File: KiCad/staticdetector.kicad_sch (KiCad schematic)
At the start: 15 parts, among them J1 Conn_01x04, Q1 Q_NMOS_GDS_2SK4033, Q2 Q_NPN_BEC_2PD601ART, Q3 Q_NPN_BCE_2SCR533P, SW1 SW_Push

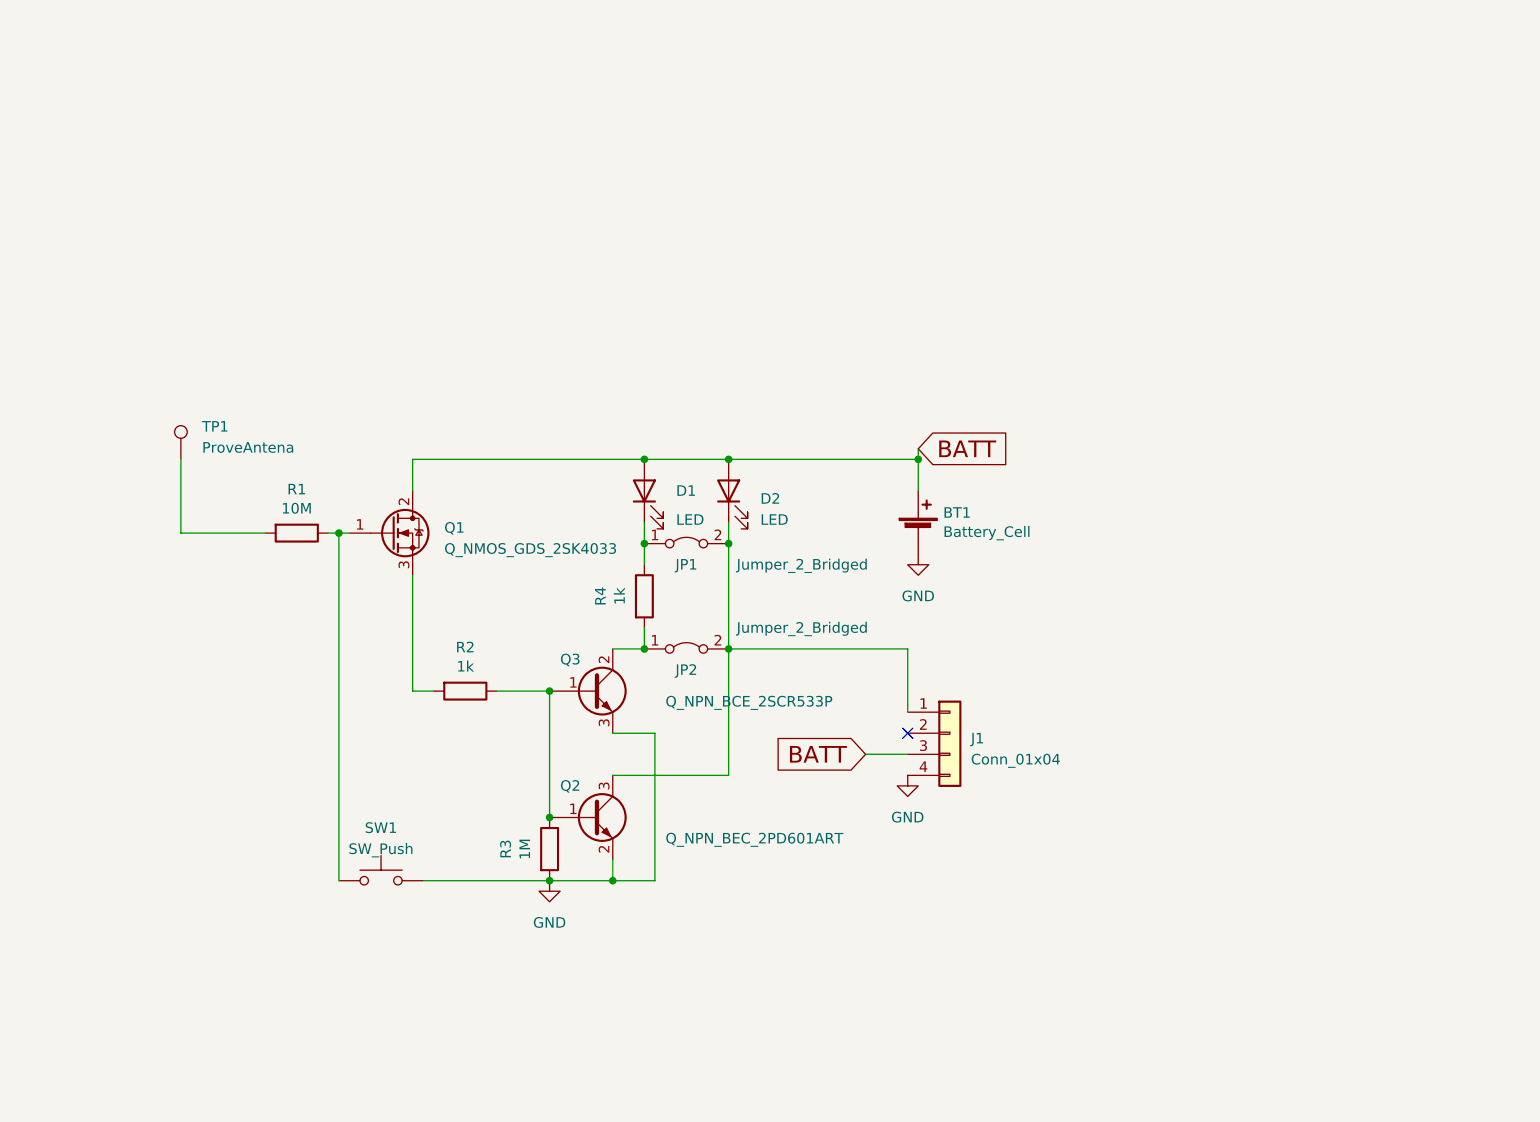
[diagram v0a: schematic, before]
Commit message: change file to OPAMP version
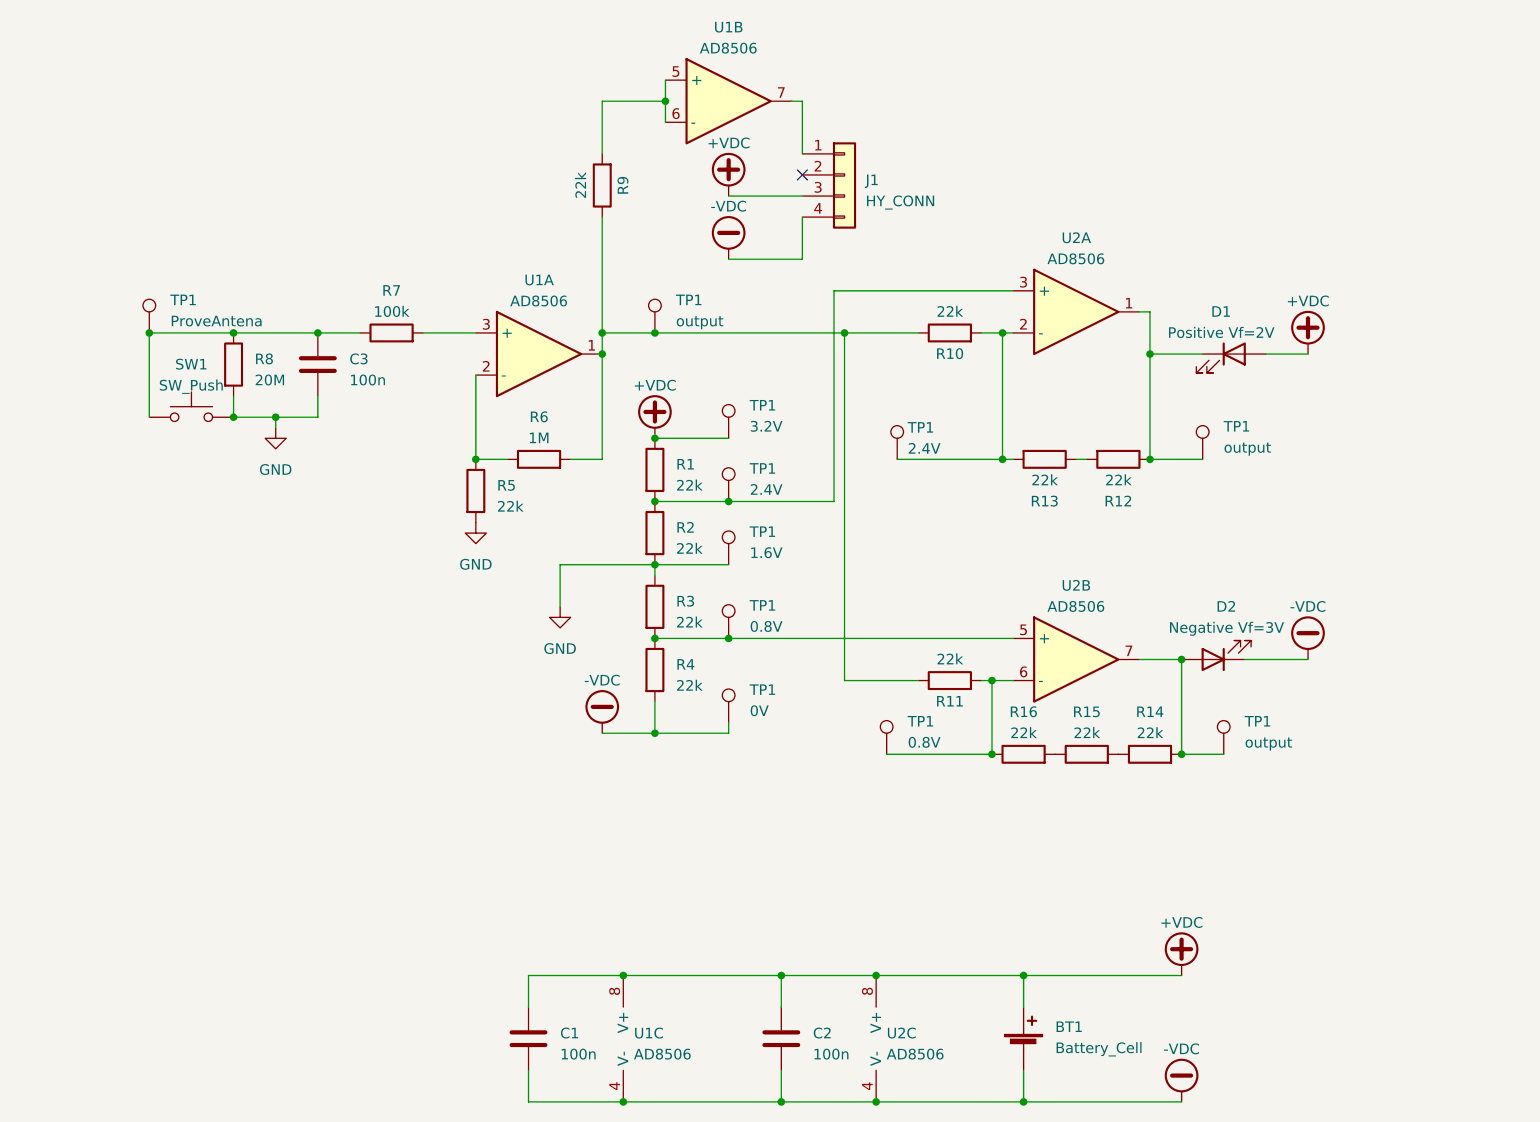
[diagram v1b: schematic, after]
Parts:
- removed JP1, JP2: Jumper_2_Bridged, Jumper:SolderJumper-2_P1.3mm_Bridged_RoundedPad1.0x1.5mm, symbol Jumper:Jumper_2_Bridged
- removed Q1: Q_NMOS_GDS_2SK4033, Package_TO_SOT_SMD:TO-252-2, symbol Device:Q_NMOS_GDS
- removed Q2: Q_NPN_BEC_2PD601ART, Package_TO_SOT_SMD:SOT-23W, symbol Device:Q_NPN_BEC
- removed Q3: Q_NPN_BCE_2SCR533P, Package_TO_SOT_SMD:SOT-89-3, symbol Device:Q_NPN_BCE
- removed TP1: ProveAntena, TestPoint:TestPoint_Pad_D4.0mm, symbol Connector:TestPoint
- added C1, C2, C3: 100n, Capacitor_SMD:C_1206_3216Metric_Pad1.33x1.80mm_HandSolder, symbol Device:C
- added R10, R11, R12, R13, R14, R15, R16, R5, R9: 22k, Resistor_SMD:R_1206_3216Metric_Pad1.30x1.75mm_HandSolder, symbol Device:R
- added R6: 1M, Resistor_SMD:R_1206_3216Metric_Pad1.30x1.75mm_HandSolder, symbol Device:R
- added R7: 100k, Resistor_SMD:R_1206_3216Metric_Pad1.30x1.75mm_HandSolder, symbol Device:R
- added R8: 20M, Resistor_SMD:R_1206_3216Metric_Pad1.30x1.75mm_HandSolder, symbol Device:R
- added TP1 (x2): 0.8V, TestPoint:TestPoint_Loop_D1.80mm_Drill1.0mm_Beaded, symbol Connector:TestPoint
- added TP1: ProveAntena, TestPoint:TestPoint_Pad_D4.0mm, symbol Connector:TestPoint
- added TP1: 1.6V, TestPoint:TestPoint_Loop_D2.50mm_Drill1.85mm, symbol Connector:TestPoint
- added TP1 (x2): 2.4V, TestPoint:TestPoint_Loop_D1.80mm_Drill1.0mm_Beaded, symbol Connector:TestPoint
- added TP1: 3.2V, TestPoint:TestPoint_Loop_D1.80mm_Drill1.0mm_Beaded, symbol Connector:TestPoint
- added TP1: 0V, TestPoint:TestPoint_Loop_D2.50mm_Drill1.85mm, symbol Connector:TestPoint
- added TP1 (x3): output, TestPoint:TestPoint_Loop_D1.80mm_Drill1.0mm_Beaded, symbol Connector:TestPoint
- added U1, U2: AD8506, Package_DIP:DIP-8_W8.89mm_SMDSocket_LongPads, symbol Device:Opamp_Dual
- BT1: footprint Battery:BatteryHolder_Keystone_3008_1x2450 -> Battery:BatteryHolder_Keystone_3002_1x2032
- D1: value LED -> Positive Vf=2V; footprint LED_SMD:LED_1206_3216Metric -> LED_SMD:LED_1206_3216Metric_Pad1.42x1.75mm_HandSolder
- D2: value LED -> Negative Vf=3V; footprint LED_SMD:LED_1206_3216Metric -> LED_SMD:LED_1206_3216Metric_Pad1.42x1.75mm_HandSolder
- J1: value Conn_01x04 -> HY_CONN
- R1: value 10M -> 22k; footprint Resistor_SMD:R_1206_3216Metric -> Resistor_SMD:R_1206_3216Metric_Pad1.30x1.75mm_HandSolder
- R2, R4: value 1k -> 22k; footprint Resistor_SMD:R_1206_3216Metric -> Resistor_SMD:R_1206_3216Metric_Pad1.30x1.75mm_HandSolder
- R3: value 1M -> 22k; footprint Resistor_SMD:R_1206_3216Metric -> Resistor_SMD:R_1206_3216Metric_Pad1.30x1.75mm_HandSolder
- SW1: footprint Button_Switch_SMD:SW_SPST_EVQQ2 -> Button_Switch_THT:SW_PUSH_6mm
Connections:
- net GND: now also R2.2, R3.1, SW1.2, C3.2, R5.2, R8.2, TP1.1; no longer BT1.2 (-), J1.4 (Pin_4), R3.2, SW1.1
- net +VDC: now reaches R1.1
- net +VDC: now also BT1.1 (+), D1.2 (A), J1.3 (Pin_3), C1.1, C2.1, TP1.1, U1.8 (V+), U2.8 (V+); no longer SW1.2
- net at R1.2: now also R2.1, TP1.1, U2.3 (+)
- net at J1.1 (Pin_1): now also U1.7; no longer D2.1 (K)
- net -VDC: now reaches R4.2
- net -VDC: now also BT1.2 (-), D2.1 (K), J1.4 (Pin_4), C1.2, C2.2, TP1.1, U1.4 (V-), U2.4 (V-)
- net at D1.1 (K): now also R12.1, TP1.1, U2.1; no longer R4.1
- removed net BATT: BT1.1 (+), D1.2 (A), D2.2 (A), J1.3 (Pin_3)
- new net: C3.1, R7.1, R8.1, SW1.1, TP1.1
- new net: R5.1, R6.1, U1.2 (-)
- new net: R12.2, R13.1
- new net: R10.2, R13.2, TP1.1, U2.2 (-)
- new net: R7.2, U1.3 (+)
- new net: R3.2, R4.1, TP1.1, U2.5 (+)
- new net: R10.1, R11.1, R6.2, R9.1, TP1.1, U1.1
- new net: R11.2, R16.1, TP1.1, U2.6 (-)
- new net: R15.1, R16.2
- new net: R9.2, U1.5 (+), U1.6 (-)
- new net: R14.1, R15.2
- new net: D2.2 (A), R14.2, TP1.1, U2.7

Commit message: change schematics
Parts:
- added D1: Positive Vf=2V, LED_SMD:LED_1206_3216Metric_Pad1.42x1.75mm_HandSolder, symbol Device:LED
- added D2: Negative Vf=3V, LED_SMD:LED_1206_3216Metric_Pad1.42x1.75mm_HandSolder, symbol Device:LED
- added R14 (x2): 22k, Resistor_SMD:R_1206_3216Metric_Pad1.30x1.75mm_HandSolder, symbol Device:R
- R8: value 20M -> 100M
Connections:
- net +VDC: now also D1.2 (A)
- net -VDC: now also D2.1 (K)
- net at R12.1, TP1.1, U2.1: now also D1.1 (K), R14.1; no longer D1.1 (K)
- net at R14.2, TP1.1, U2.7: now also D2.2 (A), R14.1; no longer D2.2 (A)
- new net: D1.1 (K), R14.2
- new net: D2.2 (A), R14.2
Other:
- moved on the sheet: C3, D1, D2, J1, R5, R6, R7, R8, R9, SW1, TP1, U1A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
